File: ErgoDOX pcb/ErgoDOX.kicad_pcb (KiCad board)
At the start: 2 copper layers, 182.8 x 158.9 mm, 76 parts, among them J1 USB, J2 3.5mm, J3 JMP, J4 JMP, SW0:10 SW0:3, SW0:11 SW0:2, SW0:12 SW0:1, SW0:7 SW0:6, SW0:8 SW0:5, SW0:9 SW0:4, SW1:10 SW1:3, SW1:11 SW1:2, SW1:12 SW1:1, SW1:13 SW1:0, SW1:9 SW1:4, SW2:10 SW2:3, SW2:11 SW2:2, SW2:12 SW2:1, SW2:13 SW2:0, SW2:7 SW2:6, SW2:8 SW2:5, SW2:9 SW2:4, SW3:10 SW3:3, SW3:11 SW3:2, SW3:12 SW3:1, SW3:13 SW3:0, SW3:8 SW3:5, SW3:9 SW3:4, SW4:10 SW4:3, SW4:11 SW4:2, SW4:12 SW4:1, SW4:13 SW4:0, SW4:7 SW4:6, SW4:8 SW4:5, SW4:9 SW4:4, SW5:10 SW5:3, SW5:11 SW5:2, SW5:12 SW5:1, SW5:13 SW5:0, SW5:7 SW5:6, SW5:8 SW5:5, SW5:9 SW5:4, U1 TEENSY2.0, U2 MCP23018

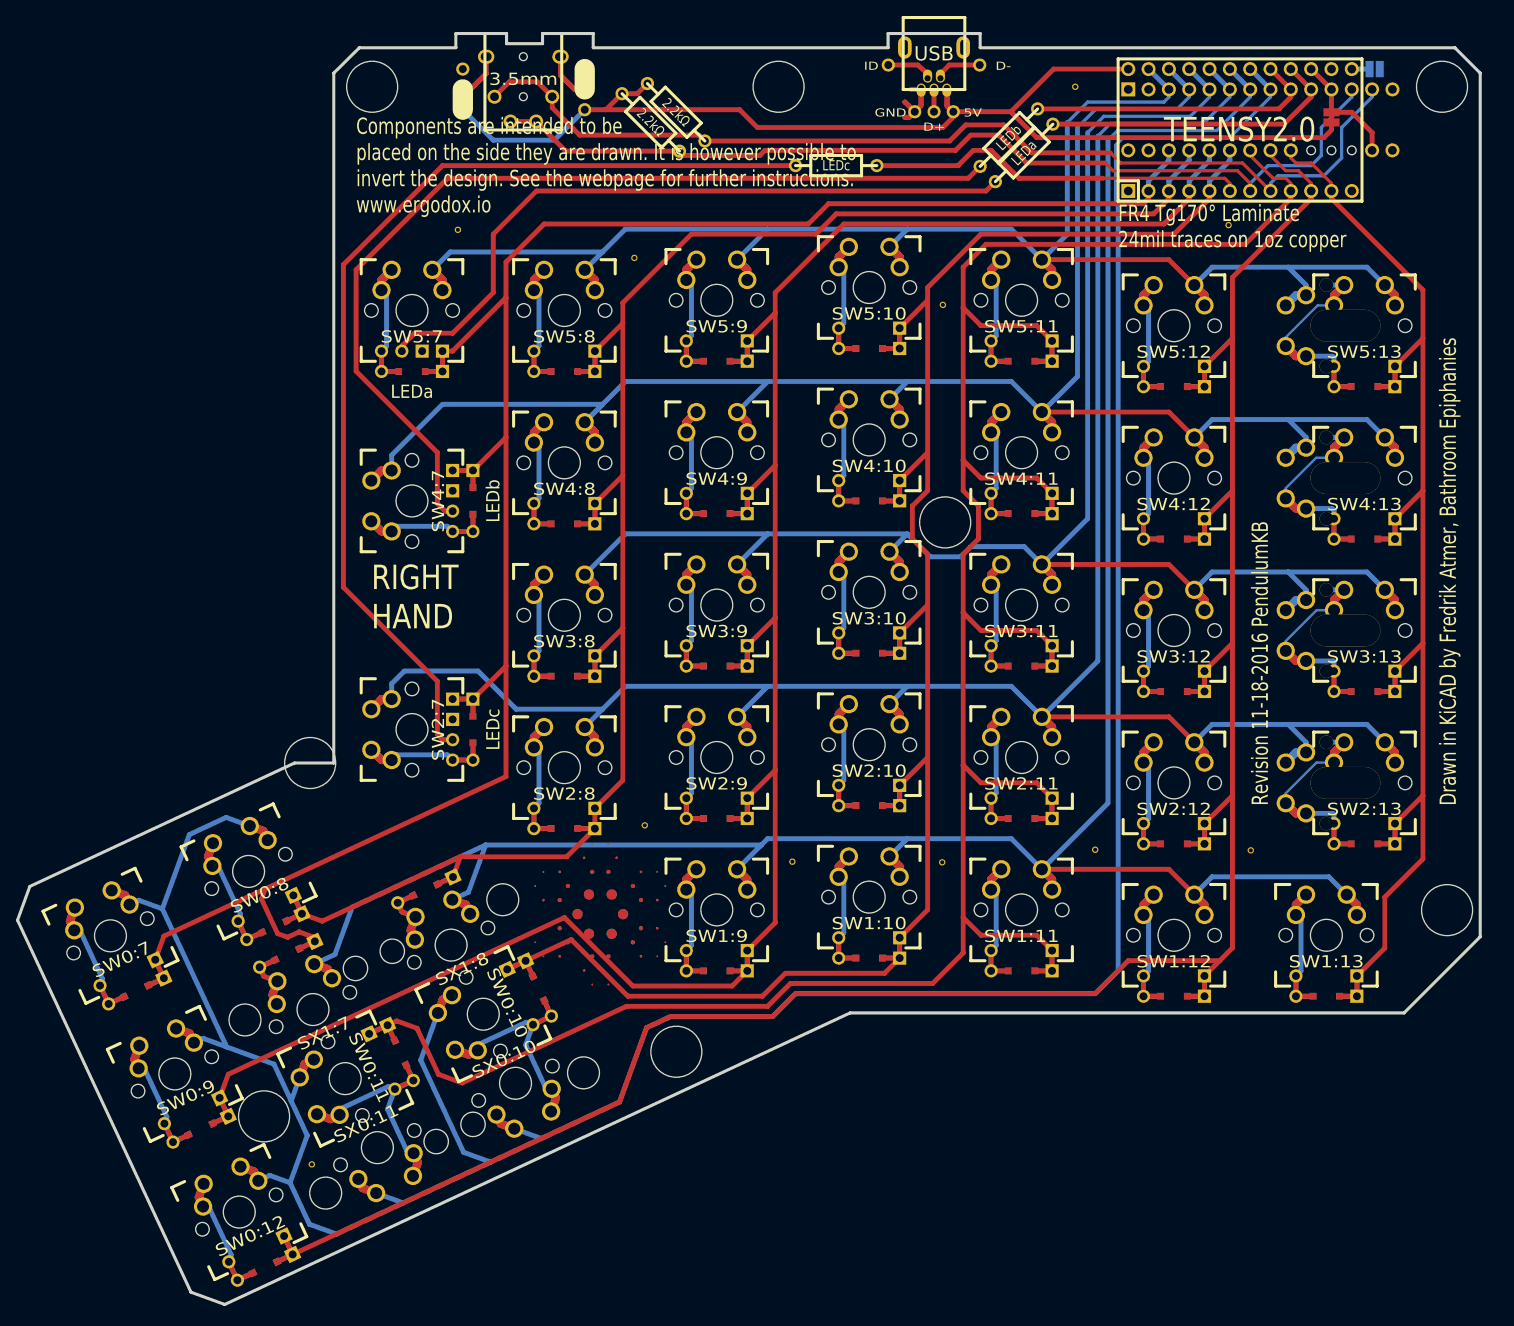
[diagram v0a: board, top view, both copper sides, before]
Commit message: Adding support for reversible female USB Port and optional reset switch. This will allow the right hand of the Ergodox to be flipped and used as the left hand. In this scenario the teensy should be soldered with its bottom facing up on the top of the left hand PCB. Because doing this obscures the teensy mounted reset button, I have added pads for an optional reset switch that can be used from the bottom of a left hand only Ergodox.
Reset switch part number: OMRON B3U-1000P
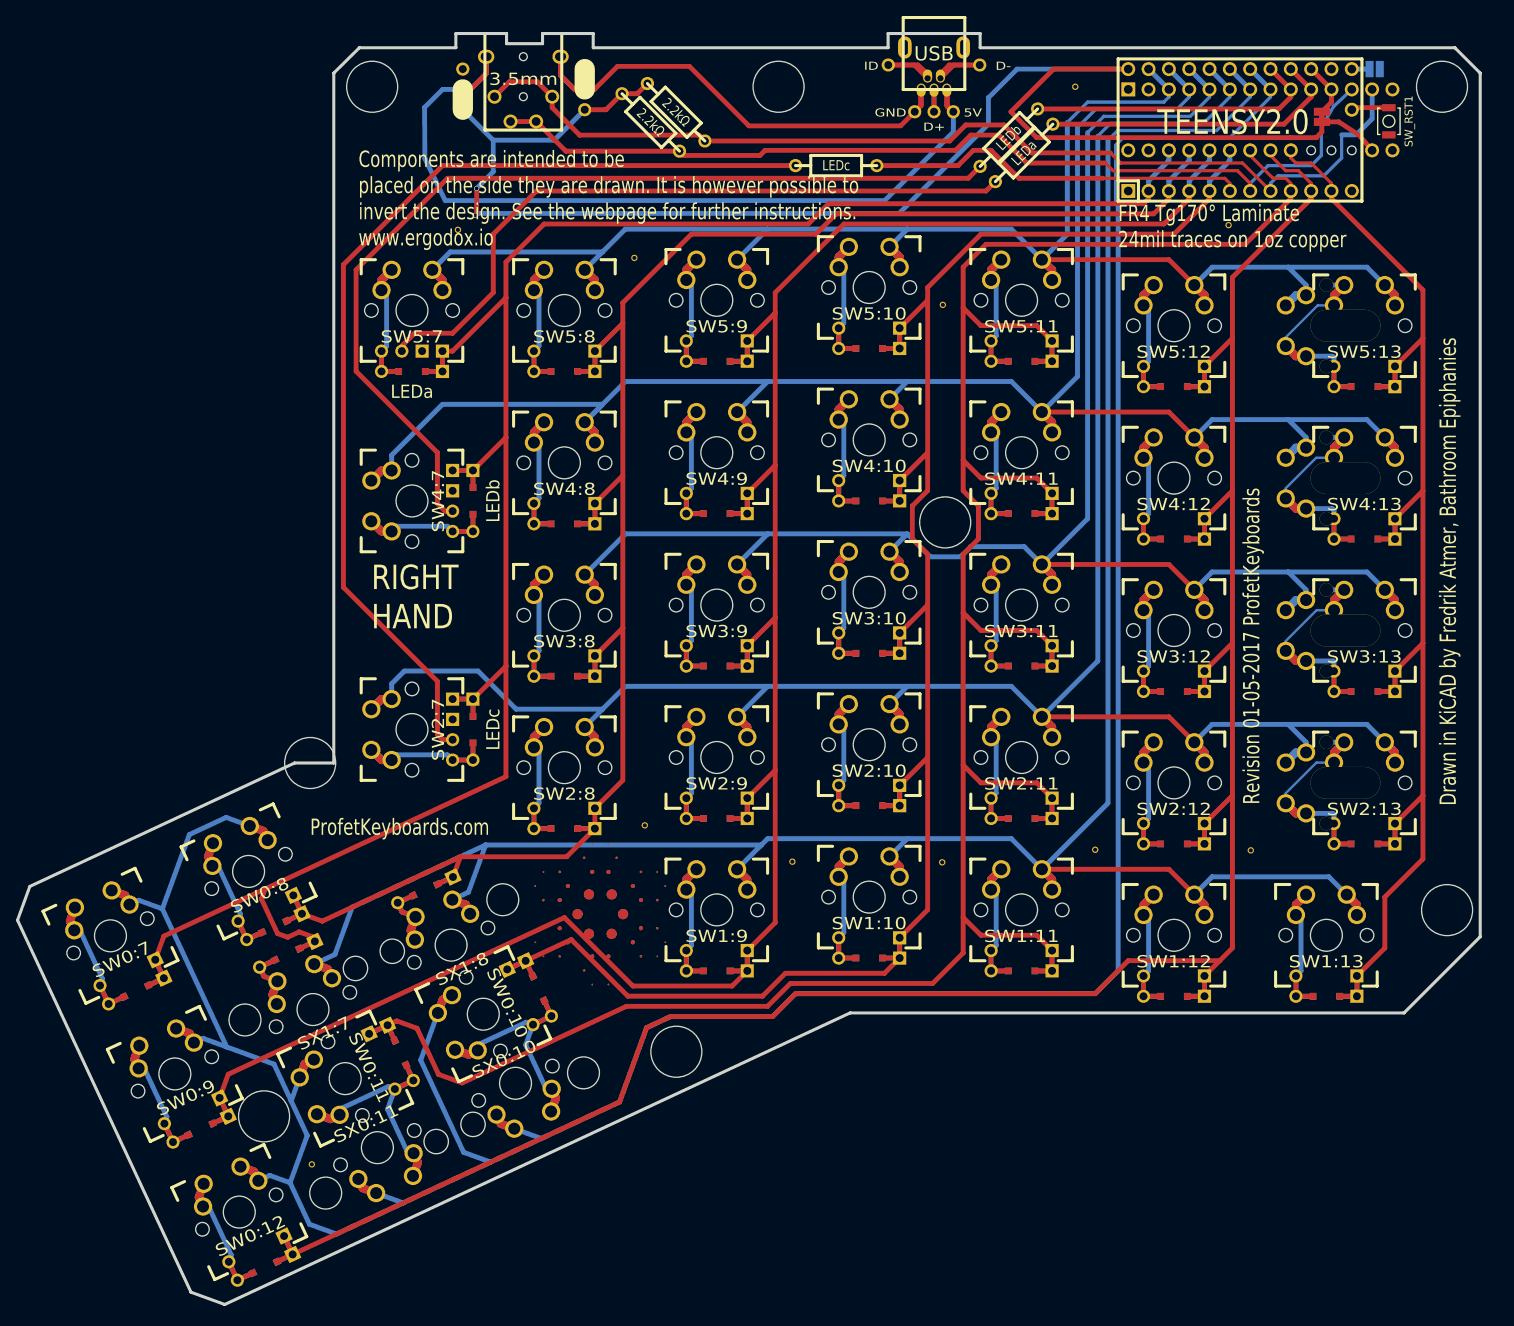
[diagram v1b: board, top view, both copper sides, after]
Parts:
- added SW_RST1: SWITCH_PUSH, Buttons_Switches_SMD:SW_SPST_B3U-1000P, F.Cu at (194.5, 41.5)
- U1: footprint TEENSY_2.0 -> ErgoDOX pcb:TEENSY_2.0_WITH_RESET
- moved JP1 1.20 mm to (186.1, 40.9)
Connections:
- J1 pad 1: VCC -> Net-(J1-Pad1)
- J1 pad 2: (no net) -> Net-(J1-Pad2)
- J1 pad 3: (no net) -> Net-(J1-Pad3)
- J1 pad 4: (no net) -> Net-(J1-Pad4)
- J1 pad 5: GND -> Net-(J1-Pad5)
- J2 pad 1: N-000003 -> Net-(J1-Pad5)
- J2 pad 4: N-000001 -> Net-(J1-Pad1)
- J3 pad 2: N-000003 -> Net-(J1-Pad5)
- J4 pad 2: N-000001 -> Net-(J1-Pad1)
- U1 pad 12: (no net) -> Net-(U1-Pad12)
- U1 pad 19: (no net) -> Net-(U1-Pad19)
- U2 pad 10: (no net) -> /LED_A
- U2 pad 14: (no net) -> Net-(U2-Pad14)
- U2 pad 17: (no net) -> Net-(U2-Pad17)
- U2 pad 18: (no net) -> Net-(U2-Pad18)
- U2 pad 19: (no net) -> Net-(U2-Pad19)
- U2 pad 27: (no net) -> Net-(U2-Pad27)
- U2 pad 28: (no net) -> Net-(U2-Pad28)
- U2 pad 9: (no net) -> /LED_B
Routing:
- net Net-(J1-Pad1): track 0.00 -> 102.6 mm
- net Net-(J1-Pad5): track 0.00 -> 62.3 mm
- net VCC: track 160.4 -> 204.8 mm, vias 0 -> 2
- net N-000003: track 12.2 -> 0.00 mm
- net N-000001: track 11.7 -> 0.00 mm
- net GND: track 13.5 -> 2.22 mm
- net Net-(J1-Pad4): track 0.00 -> 5.60 mm
- net Net-(J1-Pad2): track 0.00 -> 5.60 mm
- net /RST: track 0.00 -> 4.74 mm
- net Net-(J1-Pad3): track 0.00 -> 2.98 mm
- net /SDAM: track 127.2 -> 128.3 mm
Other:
- board text added: "ProfetKeyboards.com"
- board text added: "Revision 01-05-2017 ProfetKeyboards"
- board text removed: "Revision 11-18-2016 PendulumKB"

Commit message: wip
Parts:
- removed STAR_1: STAR_FRONT, ErgoDOX pcb:STAR
- removed STAR_2: STAR_BACK, ErgoDOX pcb:STAR
- SW0:10, SW0:11, SW0:12, SW0:7, SW0:8, SW0:9, SW1:10, SW1:11, SW1:12, SW1:13, SW1:9, SW2:10, SW2:11, SW2:12, SW2:7, SW2:8, SW2:9, SW3:10, SW3:11, SW3:12, SW3:8, SW3:9, SW4:10, SW4:11, SW4:12, SW4:7, SW4:8, SW4:9, SW5:10, SW5:11, SW5:12, SW5:7, SW5:8, SW5:9: footprint ErgoDOX pcb:MX_FLIP_DIODE -> ErgoDOX pcb:SW_Hotswap_Kailh_MX
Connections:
- SX0:10 pad 1: /ROW0 -> /ROW1
- SX0:11 pad 1: /ROW0 -> /ROW1
- U1 pad 23: /ROW0 -> /ROW1
- U2 pad 8: /ROW0 -> /ROW1
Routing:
- net /ROW1: track 318.2 -> 704.5 mm, vias 0 -> 2
- net /ROW0: track 404.2 -> 18.4 mm
- net /COL6: track 259.5 -> 190.2 mm
- net /ROW5: track 225.1 -> 206.1 mm, vias 0 -> 4
- net /COL5: track 225.8 -> 207.4 mm
- net /COL4: track 274.3 -> 290.3 mm
- net Net-(LED_B1-Pad1): track 119.1 -> 104.3 mm, vias 0 -> 2
- net /COL10: track 233.7 -> 244.6 mm
- net Net-(SW5:7-Pad2): track 19.4 -> 25.0 mm, vias 0 -> 1
- net Net-(SW2:7-Pad2): track 19.4 -> 24.1 mm, vias 0 -> 1
- net Net-(SW4:7-Pad2): track 19.4 -> 24.1 mm, vias 0 -> 1
- net /COL11: track 316.5 -> 320.9 mm
- net /ROW3: track 238.7 -> 234.6 mm, vias 0 -> 3
- net /ROW4: track 257.4 -> 260.8 mm, vias 0 -> 4
- net Net-(LED_A1-Pad1): track 87.6 -> 89.2 mm
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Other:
- net class Default removed

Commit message: some progress
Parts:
- SW2:13, SW3:13, SW4:13, SW5:13: footprint ErgoDOX pcb:MX_FLIP_XX -> ErgoDOX pcb:MX_FLIP_HOTSWAP
- moved STITCHING_VIA 2.08 mm to (122.0, 134.4)
- moved SW4:9 2.08 mm to (112.5, 83.3)
- moved S1 2.08 mm to (66.1, 161.6)
- moved SW0:11 2.08 mm to (66.1, 161.6)
- moved SW4:11 2.08 mm to (150.6, 83.3)
- moved SW2:8 2.08 mm to (93.5, 122.7)
- moved SW5:9 2.08 mm to (112.5, 64.3)
- moved LED_C1 2.08 mm to (74.4, 117.9)
- moved SW2:7 2.08 mm to (74.4, 117.9)
- moved J4 2.08 mm to (80.8, 37.9)
- moved SW0:7 2.08 mm to (36.7, 143.7)
- moved SW1:13 2.08 mm to (188.7, 143.6)
- moved SW3:13 2.08 mm to (193.5, 105.5)
- moved SW4:13 2.08 mm to (193.5, 86.5)
- moved SX1:8 2.08 mm to (79.3, 144.9)
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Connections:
- SW2:13 pad 2: Net-(SW2:13-Pad2) -> /ROW2
- SW3:13 pad 2: Net-(SW3:13-Pad2) -> /ROW3
- SW4:13 pad 2: Net-(SW4:13-Pad2) -> /ROW4
- SW5:13 pad 2: Net-(SW5:13-Pad2) -> /ROW5
- SX0:10 pad 1: /ROW1 -> /ROW0
- SX0:11 pad 1: /ROW1 -> /ROW0
- U1 pad 23: /ROW1 -> /ROW0
- U2 pad 8: /ROW1 -> /ROW0
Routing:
- net /ROW0: track 18.4 -> 462.6 mm, vias 0 -> 6
- net /ROW1: track 704.5 -> 316.9 mm, vias 2 -> 5
- net /COL6: track 190.2 -> 286.1 mm, vias 0 -> 1
- net /COL4: track 290.3 -> 339.3 mm, vias 0 -> 2
- net /COL5: track 207.4 -> 252.7 mm, vias 0 -> 2
- net /ROW5: track 206.1 -> 236.4 mm, vias 4 -> 9
- net Net-(SW5:13-Pad2): track 38.0 -> 56.3 mm, vias 0 -> 2
- net Net-(SW4:13-Pad2): track 38.1 -> 55.5 mm, vias 0 -> 1
- net Net-(SW3:13-Pad2): track 38.1 -> 55.5 mm, vias 0 -> 1
- net Net-(SW2:13-Pad2): track 37.7 -> 54.6 mm, vias 0 -> 1
- net /COL1: track 291.8 -> 308.4 mm
- net /COL11: track 320.9 -> 337.2 mm, vias 0 -> 2
- net /COL0: track 159.7 -> 168.3 mm
- net /ROW2: track 295.9 -> 290.2 mm, vias 4 -> 8
- net Net-(SW2:7-Pad2): track 24.1 -> 20.1 mm
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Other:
- board text added: "Drawn in KiCAD by Zeeb"
- board text removed: "Drawn in KiCAD by Fredrik Atmer, Bathroom Epiphanies"
- board text removed: "ProfetKeyboards.com"
